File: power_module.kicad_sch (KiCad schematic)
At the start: 42 parts, among them IC10 LM2678SX-ADJ/NOPB, IC5 LM2678SX-ADJ/NOPB, IC7 LT8609AEDDM#PBF, IC9 LM2678SX-ADJ/NOPB, J1 Conn_01x02_Pin, J2 Conn_01x02_Pin

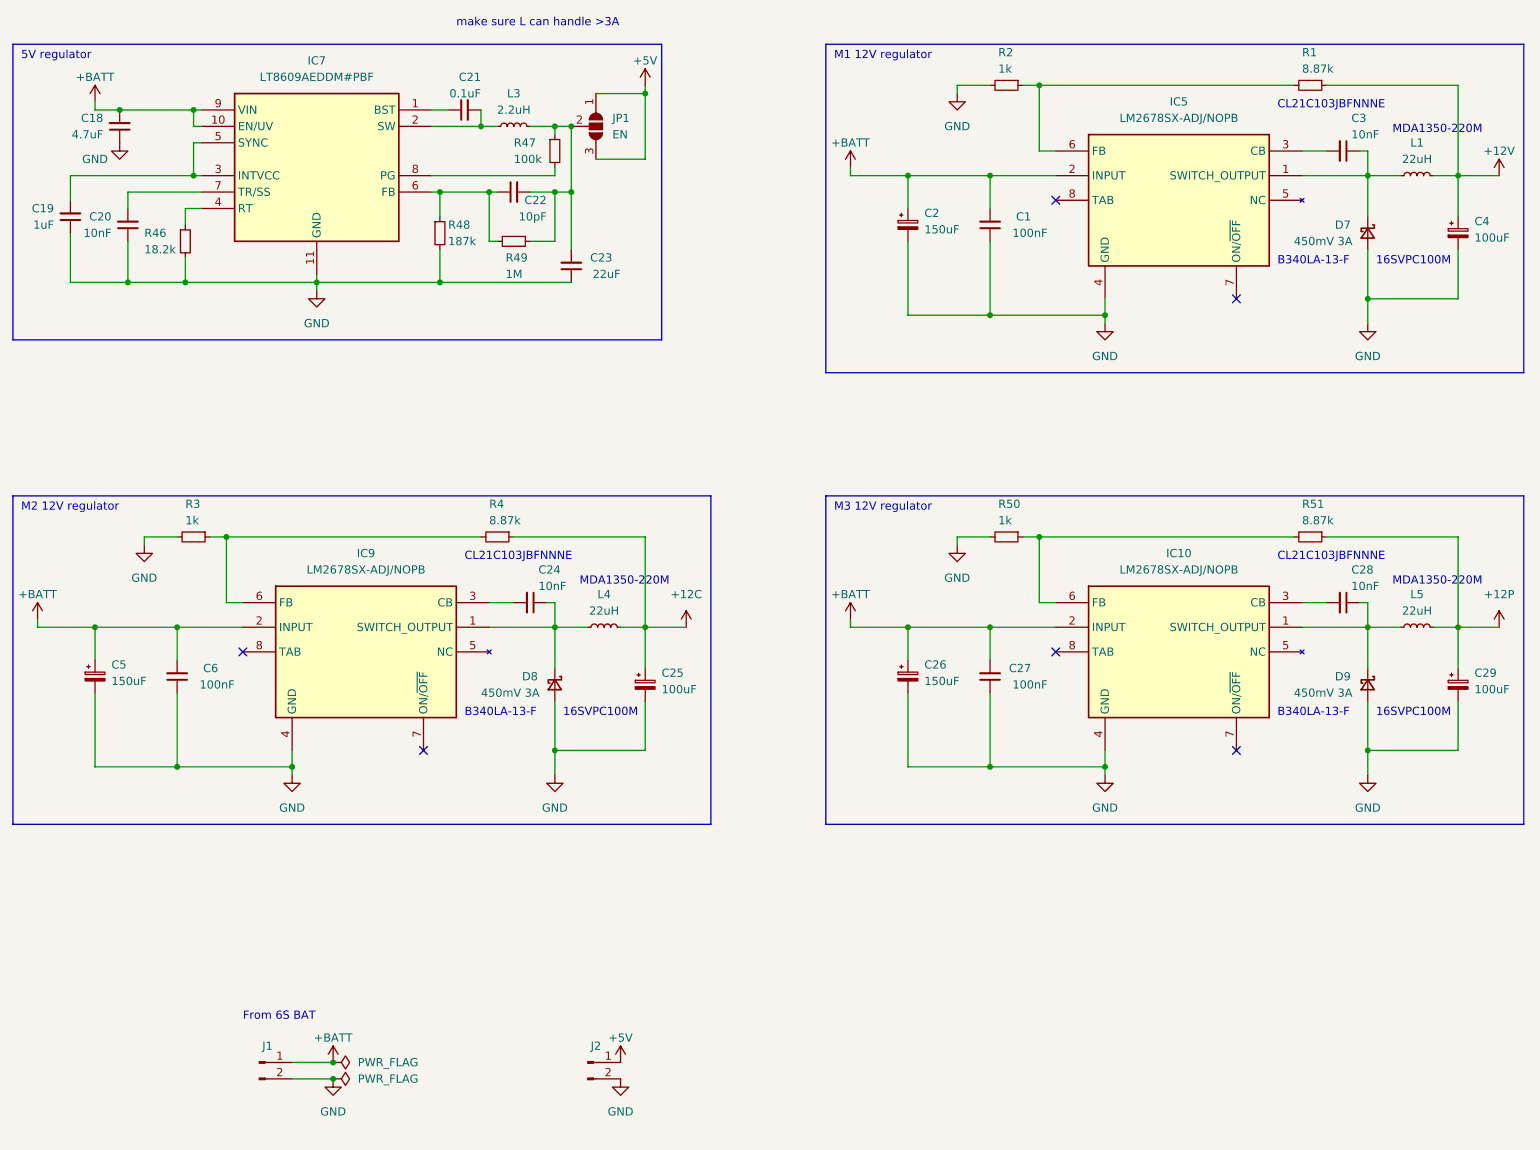
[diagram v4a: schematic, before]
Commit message: Completed full schematics
New features:
- extra 5V reg for handling camera current
- extra 12V reg for powering external LEDs
- added circuit for external emergency stop switch
- added some solder jumper for design flexibility
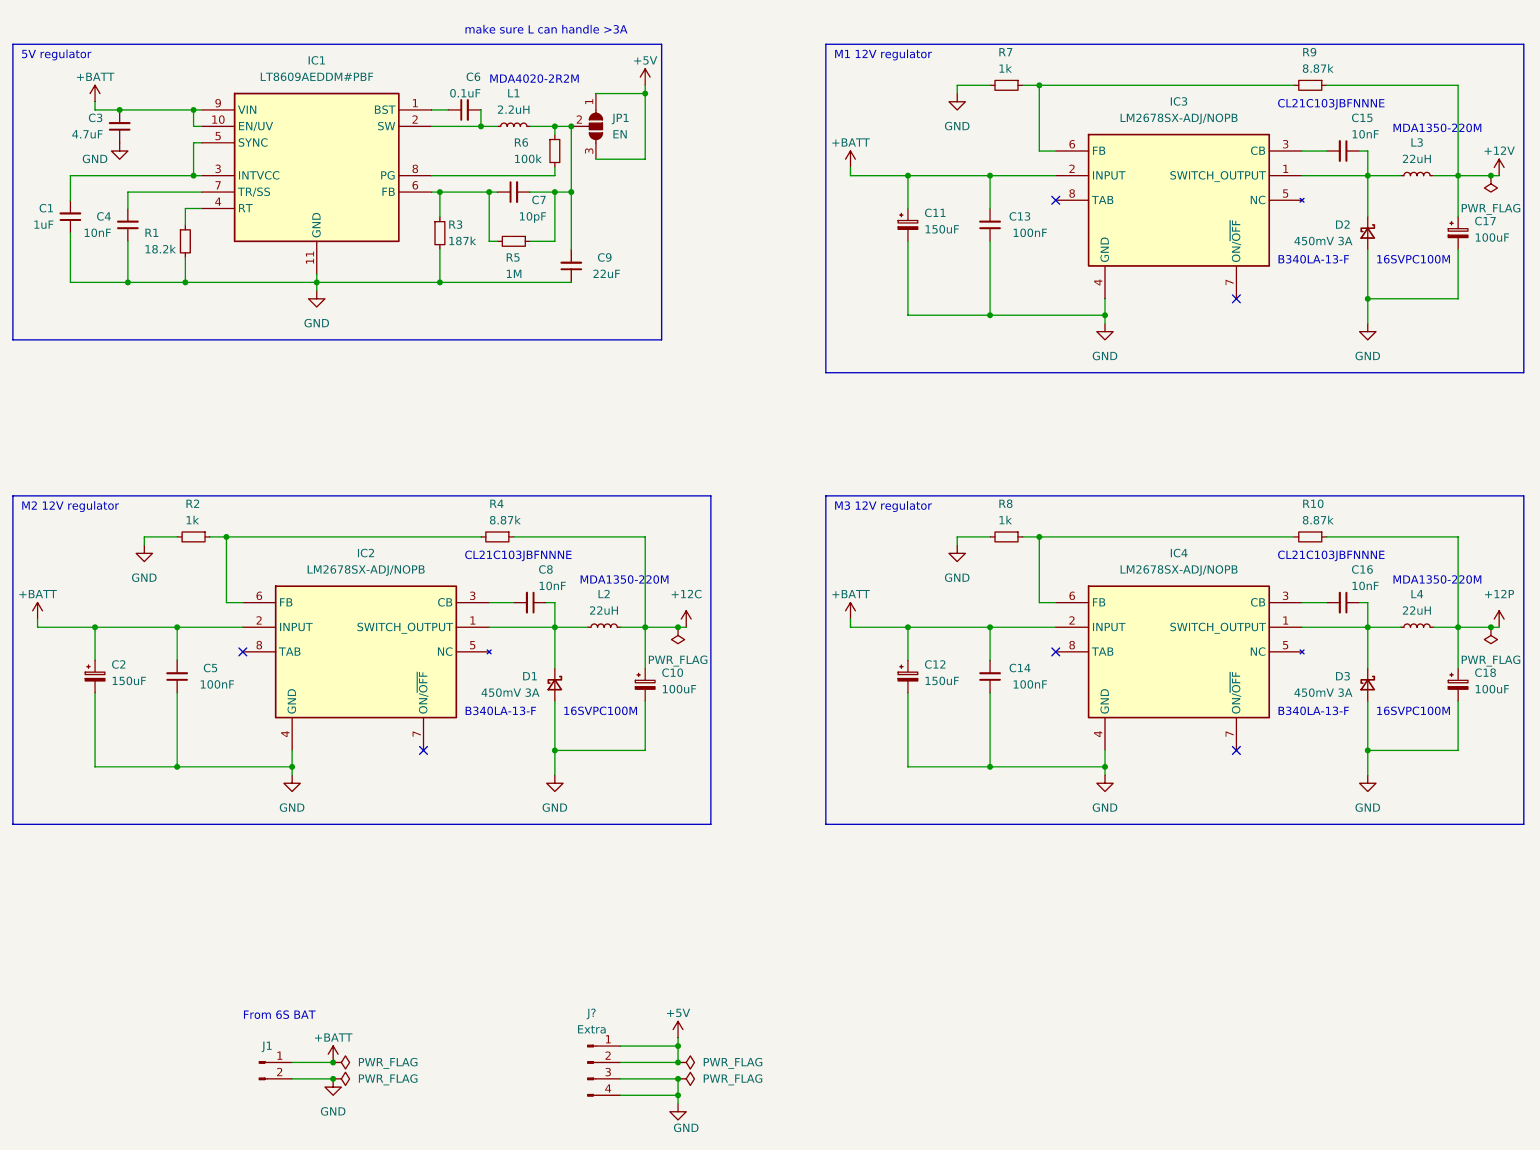
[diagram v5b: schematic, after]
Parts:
- removed J2: Conn_01x02_Pin, Connector_PinHeader_2.54mm:PinHeader_1x02_P2.54mm_Vertical, symbol Connector:Conn_01x02_Pin
- added J?: Extra, symbol Connector:Conn_01x04_Pin
- renumbered C19 to C1, C25 to C10, C2 to C11, C26 to C12, C1 to C13, C27 to C14, C3 to C15, C28 to C16, C4 to C17, C29 to C18, C5 to C2, C18 to C3, C20 to C4, C6 to C5, C21 to C6, C22 to C7, C24 to C8, C23 to C9, D8 to D1, D7 to D2, D9 to D3, IC7 to IC1, IC9 to IC2, IC5 to IC3, IC10 to IC4, L3 to L1, L4 to L2, L1 to L3, L5 to L4, R46 to R1, R51 to R10, R3 to R2, R48 to R3, R49 to R5, R47 to R6, R2 to R7, R50 to R8, R1 to R9
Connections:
- net +5V: now also J?.1 (Pin_1), J?.2 (Pin_2)
- net GND: now also J?.3 (Pin_3), J?.4 (Pin_4)
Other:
- note added: "MDA4020-2R2M"

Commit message: footprint assignment WIP
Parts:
- C1: footprint Capacitor_SMD:C_0603_1608Metric_Pad1.08x0.95mm_HandSolder -> Capacitor_SMD:C_0603_1608Metric; Part No. (none) -> TCC0603X5R105K250CT
- C3: footprint Capacitor_SMD:C_0603_1608Metric_Pad1.08x0.95mm_HandSolder -> Capacitor_SMD:C_1206_3216Metric; Part No. (none) -> CGA5L1X7R1H475KT0Y0S
- C4: footprint Capacitor_SMD:C_0603_1608Metric_Pad1.08x0.95mm_HandSolder -> Capacitor_SMD:C_0402_1005Metric; Part No. (none) -> CSA0402X7R103K500GT
- C6: footprint Capacitor_SMD:C_0603_1608Metric_Pad1.08x0.95mm_HandSolder -> Capacitor_SMD:C_0402_1005Metric; Part No. (none) -> GRM155R71H104KE14J
- C7: footprint Capacitor_SMD:C_0603_1608Metric_Pad1.08x0.95mm_HandSolder -> Capacitor_SMD:C_0603_1608Metric; Part No. (none) -> VJ0603A100JXACW1BC
- C9: footprint Capacitor_SMD:C_0603_1608Metric_Pad1.08x0.95mm_HandSolder -> Capacitor_SMD:C_1206_3216Metric; Part No. (none) -> 1206X226K100CT
- L1: Part No. (none) -> SRP4020TA-2R2M
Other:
- note removed: "MDA4020-2R2M"

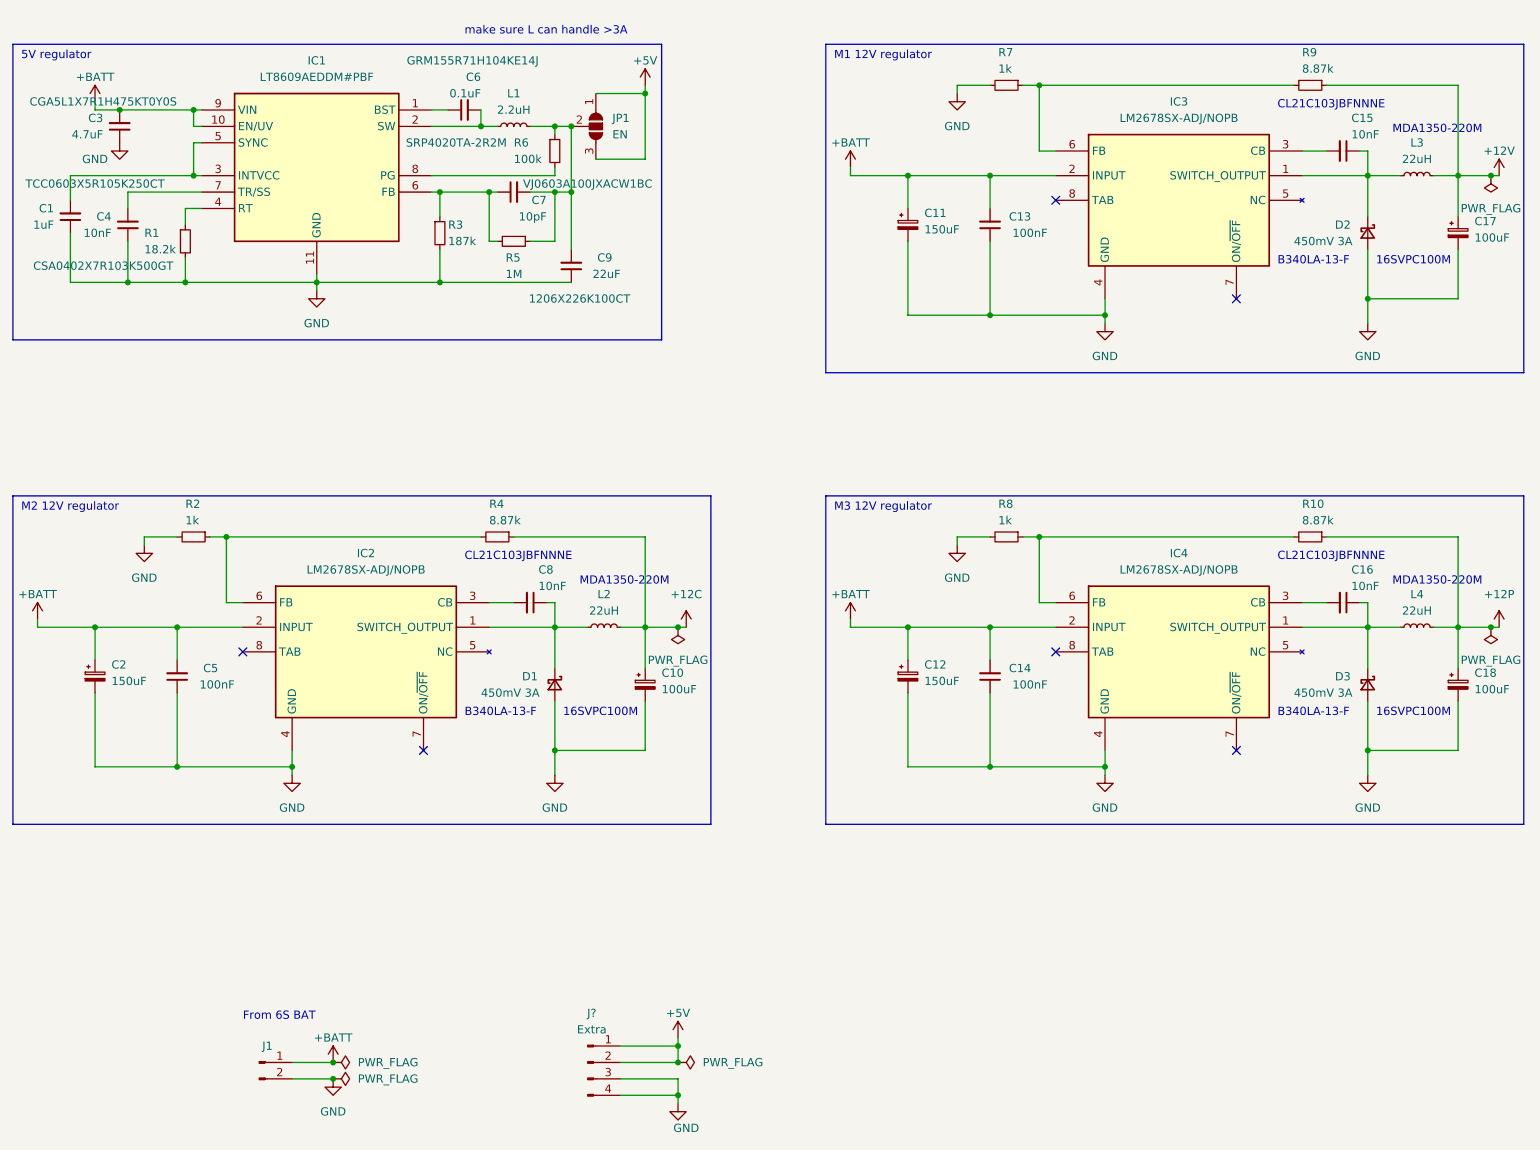
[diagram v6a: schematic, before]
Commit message: completed footprint assignments
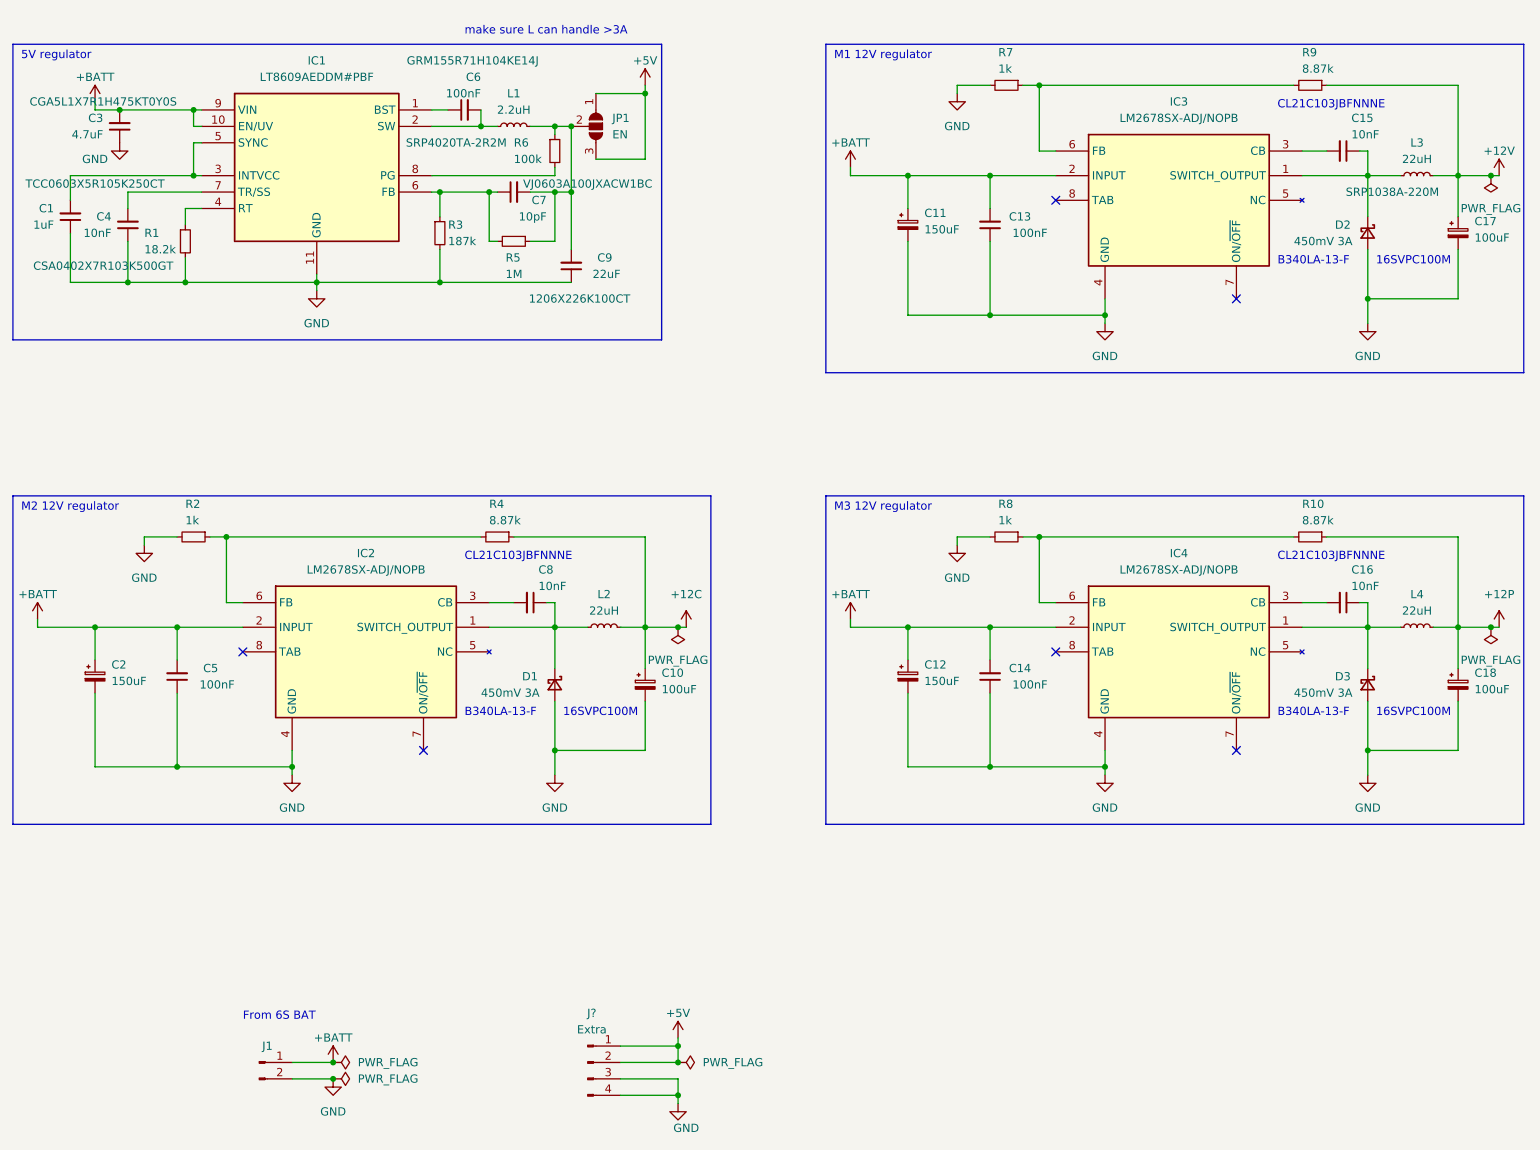
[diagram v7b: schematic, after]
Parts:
- C10, C17, C18: footprint (none) -> SamacSys_Parts:16SVF180M
- C11, C12, C2: footprint (none) -> SamacSys_Parts:EEHZT1E331UP
- C13, C14, C5: footprint Capacitor_SMD:C_0603_1608Metric_Pad1.08x0.95mm_HandSolder -> Capacitor_SMD:C_0402_1005Metric
- C15, C16, C8: footprint Capacitor_SMD:C_0603_1608Metric_Pad1.08x0.95mm_HandSolder -> Capacitor_SMD:C_0805_2012Metric
- C6: value 0.1uF -> 100nF
- D1, D2, D3: footprint (none) -> Diode_SMD:D_SMA
- J?: footprint (none) -> Connector_PinHeader_2.54mm:PinHeader_2x02_P2.54mm_Vertical
- L1: footprint LQH3NPH150MMEL:IND_LQH3NPH150MMEL -> SamacSys_Parts:INDC4441X200N
- L2, L4: footprint LQH3NPH150MMEL:IND_LQH3NPH150MMEL -> SamacSys_Parts:INDPM110100X400N
- L3: footprint LQH3NPH150MMEL:IND_LQH3NPH150MMEL -> SamacSys_Parts:INDPM110100X400N; Part No. (none) -> SRP1038A-220M
- R1: footprint Resistor_SMD:R_0805_2012Metric_Pad1.20x1.40mm_HandSolder -> Resistor_SMD:R_0603_1608Metric_Pad0.98x0.95mm_HandSolder; Part No. (none) -> CRCW060318K2FKEA
- R10, R9: footprint Resistor_SMD:R_0805_2012Metric_Pad1.20x1.40mm_HandSolder -> Resistor_SMD:R_0603_1608Metric
- R2: footprint Resistor_SMD:R_0805_2012Metric_Pad1.20x1.40mm_HandSolder -> Resistor_SMD:R_0201_0603Metric; Part No. (none) -> RC0201FR-071KL
- R3: footprint Resistor_SMD:R_0805_2012Metric_Pad1.20x1.40mm_HandSolder -> Resistor_SMD:R_0603_1608Metric; Part No. (none) -> AC0603FR-07187KL
- R4: footprint Resistor_SMD:R_0805_2012Metric_Pad1.20x1.40mm_HandSolder -> Resistor_SMD:R_0603_1608Metric; Part No. (none) -> RT0603BRE078K87L
- R5: footprint Resistor_SMD:R_0805_2012Metric_Pad1.20x1.40mm_HandSolder -> Resistor_SMD:R_0402_1005Metric; Part No. (none) -> AC0402FR-071ML
- R6, R7, R8: footprint Resistor_SMD:R_0805_2012Metric_Pad1.20x1.40mm_HandSolder -> Resistor_SMD:R_0201_0603Metric
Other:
- note removed: "MDA1350-220M"
